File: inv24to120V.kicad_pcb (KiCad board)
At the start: 2 copper layers, 237.5 x 150 mm, 161 parts, among them J1 0705530003, J10 Screw_Terminal_01x01, J12 Screw_Terminal_01x01, J2 Conn_01x02, J3 Conn_01x02, J7 Screw_Terminal_01x03, Q1 IRFZ44NPBF, Q2 IRFZ44NPBF, Q3 ZXTN2010ZTA, Q4 ZXTN2010ZTA, Q5 ZXTP2012ZTA, Q6 ZXTP2012ZTA, SW1 SW_DIP_x02, U1 ESP32-DEVKITC-32D, U10 FOD817A, U11 ACT45B-220-2P-TL003, U12 LM2576R-5.0, U13 FOD817A, U14 KIA7805AF, U15 FOD817A, U2 LM2576R-5.0, U3 ACS712ELCTR30AT, U4 ACS712ELCTR30AT, U6 ISO7340CDW, U7 ISO7340CDW, U8 AMC1300BDWVR, U9 TJA1040T

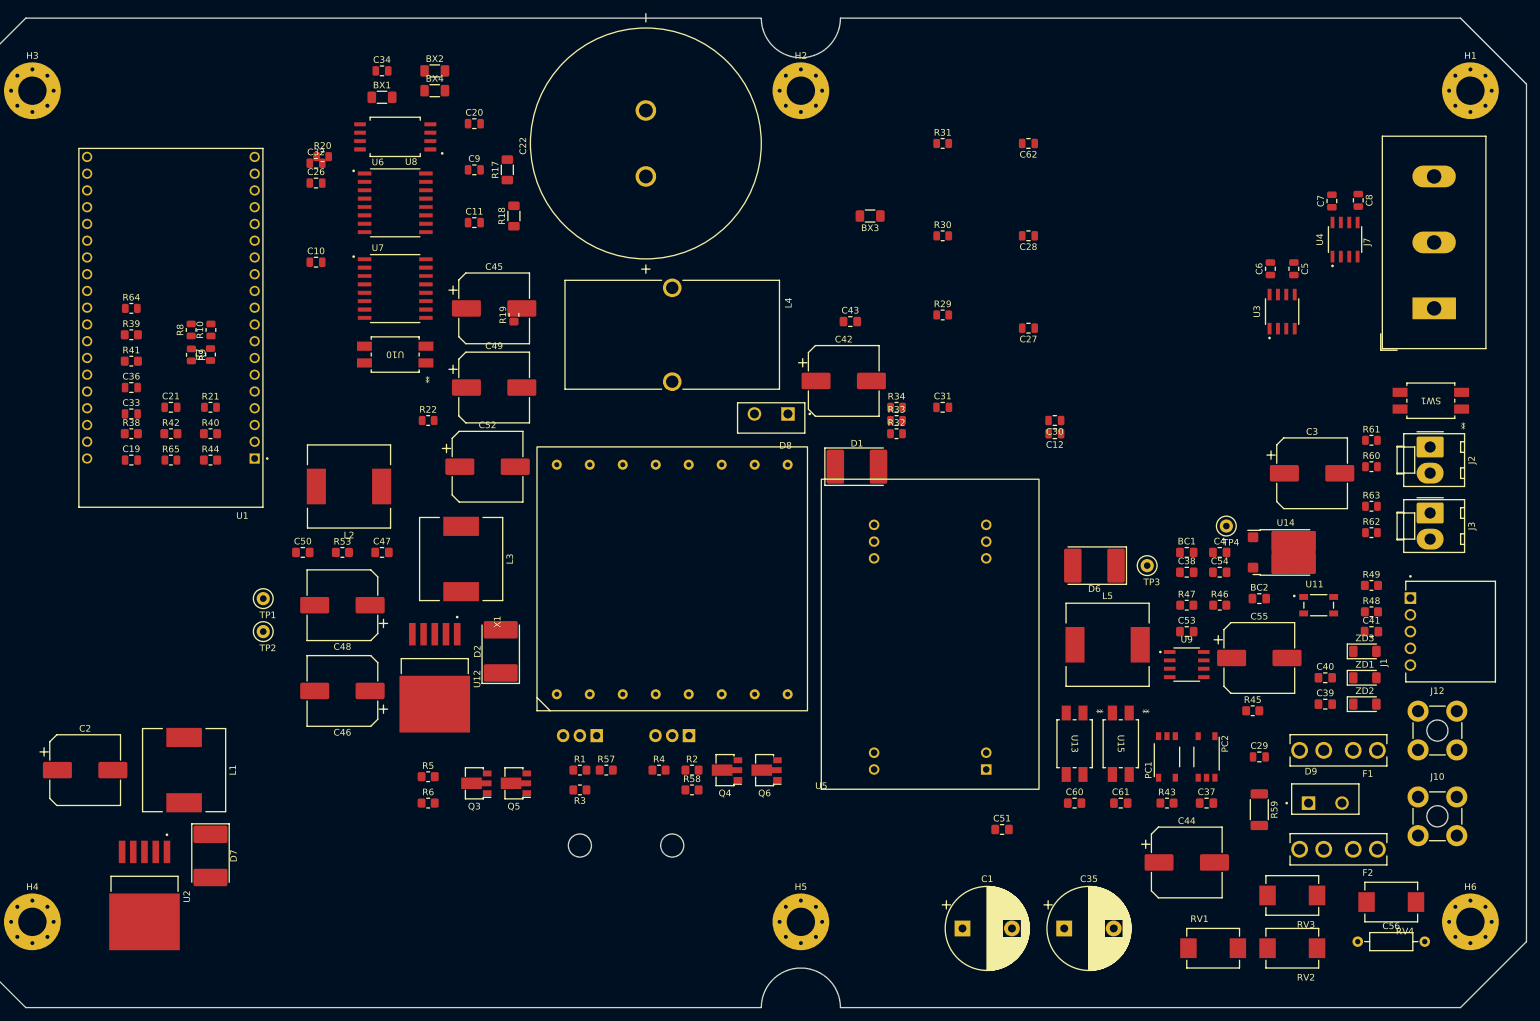
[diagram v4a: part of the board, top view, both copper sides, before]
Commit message: non isolate inverter place parts,
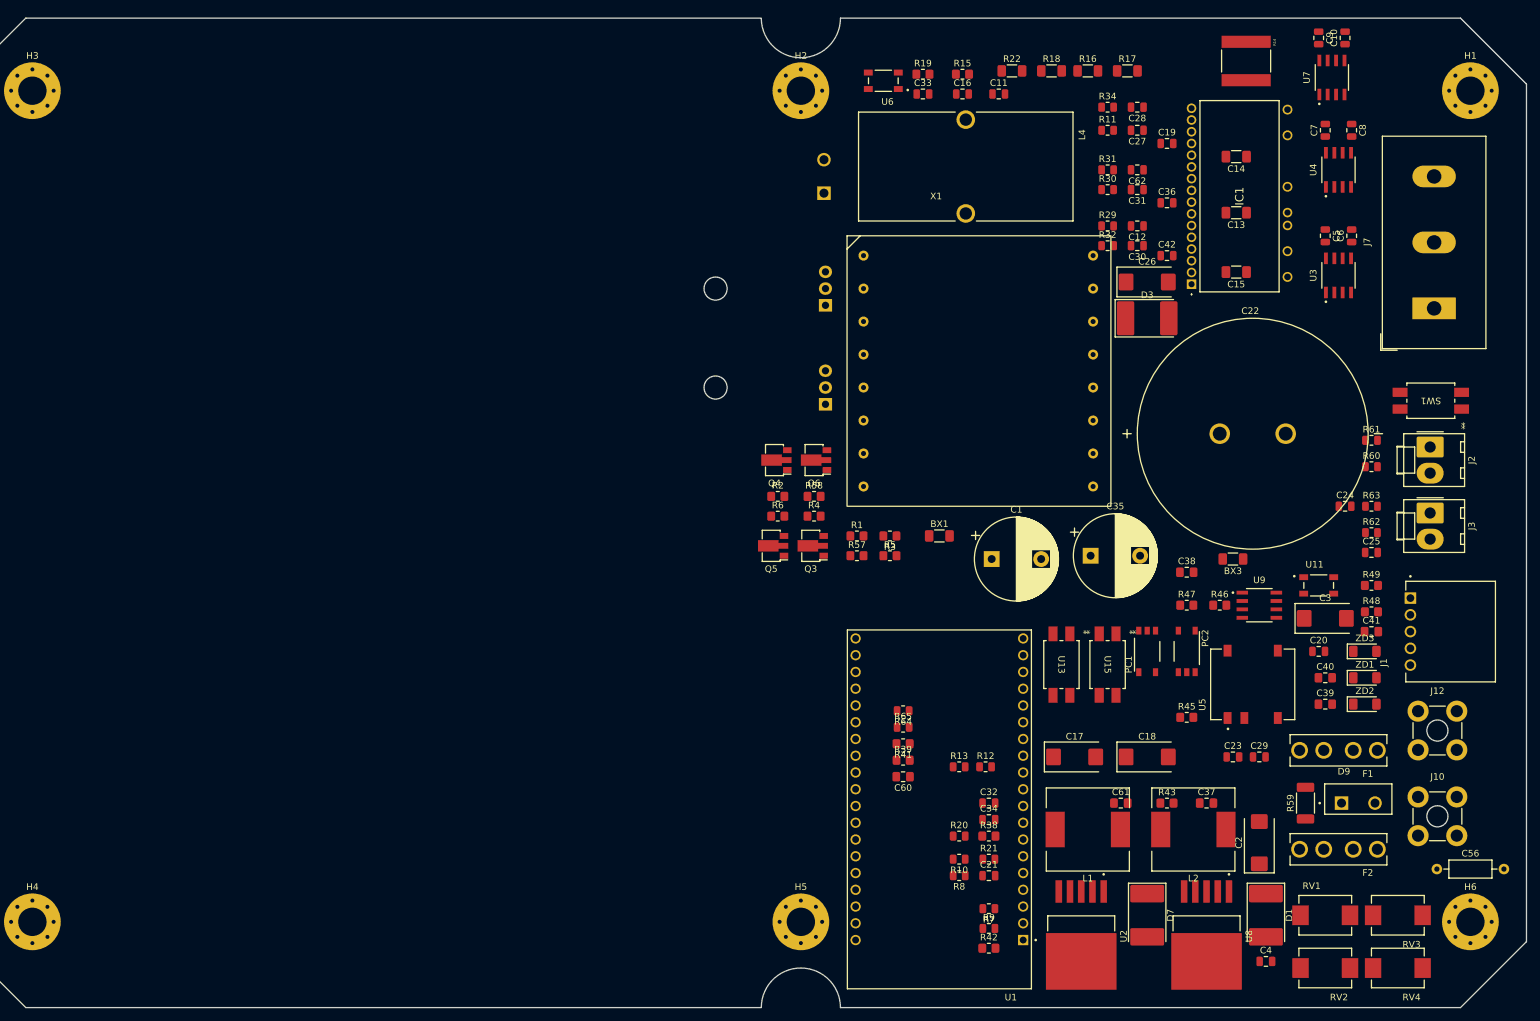
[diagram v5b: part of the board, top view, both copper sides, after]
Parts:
- removed BC1, BC2, C43, C47, C50, C51, C54: 104, Capacitor_SMD:C_0805_2012Metric_Pad1.18x1.45mm_HandSolder
- removed BX2, BX4: BLM31KN801SH1L, Resistor_SMD:R_1206_3216Metric_Pad1.30x1.75mm_HandSolder
- removed C44, C45, C46, C48, C49: 470uF/25V, Capacitor_SMD:CP_Elec_10x12.5
- removed C52, C55: 220uF/50V, Capacitor_SMD:CP_Elec_10x12.5
- removed C53: 334, Capacitor_SMD:C_0805_2012Metric_Pad1.18x1.45mm_HandSolder
- removed D2, D6: SS16, Diode_SMD:D_3220_8050Metric_Pad2.65x5.15mm_HandSolder
- removed L3, L5: 100uH, Inductor_SMD:L_12x12mm_H8mm
- removed R33: 100, Resistor_SMD:R_0805_2012Metric
- removed R40: 10K, Resistor_SMD:R_0805_2012Metric_Pad1.20x1.40mm_HandSolder
- removed R44: 4.7K, Resistor_SMD:R_0805_2012Metric_Pad1.20x1.40mm_HandSolder
- removed R53: 1k, Resistor_SMD:R_0805_2012Metric_Pad1.20x1.40mm_HandSolder
- removed TP1, TP2, TP3, TP4: TestPoint, TestPoint:TestPoint_Loop_D2.50mm_Drill1.0mm
- removed U10: FOD817A, inv24VLib:PDIP4GW_709AH_ONS-M
- removed U12: LM2576R-5.0, genCtrlPCB_Lib:VREG_TPS79625KTTR
- removed U14: KIA7805AF, Package_TO_SOT_SMD:ATPAK-2
- added C13: 10uF, Capacitor_SMD:C_1206_3216Metric_Pad1.33x1.80mm_HandSolder, F.Cu at (223.5, 44.5)
- added C14: 10uF, Capacitor_SMD:C_1206_3216Metric_Pad1.33x1.80mm_HandSolder, F.Cu at (223.5, 36.0)
- added C15: 10uF, Capacitor_SMD:C_1206_3216Metric_Pad1.33x1.80mm_HandSolder, F.Cu at (223.5, 53.5)
- added C16: 102, Capacitor_SMD:C_0805_2012Metric, F.Cu at (182.0, 26.5)
- added C17: 22uF/25V TCSCS1E226MDAR, Capacitor_Tantalum_SMD:CP_EIA-7343-31_Kemet-D_Pad2.25x2.55mm_HandSolder, F.Cu at (199.0, 127.0)
- added C18: 22uF/25V TCSCS1E226MDAR, Capacitor_Tantalum_SMD:CP_EIA-7343-31_Kemet-D_Pad2.25x2.55mm_HandSolder, F.Cu at (210.0, 127.0)
- added C23: 104, Capacitor_SMD:C_0805_2012Metric, F.Cu at (223.0, 127.0)
- added C24: 104, Capacitor_SMD:C_0805_2012Metric, F.Cu at (240.0, 89.0)
- added C25: 104, Capacitor_SMD:C_0805_2012Metric, F.Cu at (244.0, 96.0)
- added D3: SS16, Diode_SMD:D_3220_8050Metric_Pad2.65x5.15mm_HandSolder, F.Cu at (210.0, 60.5)
- added IC1: NFA50460R4B, kilib:NFA50460R4B, F.Cu at (216.7, 55.3)
- added R11: 100, Resistor_SMD:R_0805_2012Metric, F.Cu at (204.0, 32.0)
- added R12: 2K, Resistor_SMD:R_0805_2012Metric, F.Cu at (185.5, 128.5)
- added R13: 2K, Resistor_SMD:R_0805_2012Metric, F.Cu at (181.5, 128.5)
- added R14: CSS2728JT40L0, kilib:RESC6771X124N, F.Cu at (225.0, 21.5)
- added R15: 1k, Resistor_SMD:R_0805_2012Metric_Pad1.20x1.40mm_HandSolder, F.Cu at (182.0, 23.5)
- added R16: 51K, Resistor_SMD:R_1206_3216Metric_Pad1.30x1.75mm_HandSolder, F.Cu at (201.0, 23.0)
- C10, C11: value 104 -> 102
- C19, C36: value 104 -> 10uF
- C2, C3: value 470uF/25V -> 22uF/25V TCSCS1E226MDAR; footprint Capacitor_SMD:CP_Elec_10x12.5 -> Capacitor_Tantalum_SMD:CP_EIA-7343-31_Kemet-D_Pad2.25x2.55mm_HandSolder
- C26: value 104 -> 22uF/25V TCSCS1E226MDAR; footprint Capacitor_SMD:C_0805_2012Metric -> Capacitor_Tantalum_SMD:CP_EIA-7343-31_Kemet-D_Pad2.25x2.55mm_HandSolder
- C4: footprint Capacitor_SMD:C_0805_2012Metric_Pad1.18x1.45mm_HandSolder -> Capacitor_SMD:C_0805_2012Metric
- C42: value 470uF/25V -> 10uF; footprint Capacitor_SMD:CP_Elec_10x12.5 -> Capacitor_SMD:C_0805_2012Metric
- D8: moved to B.Cu
- R17, R18: value 1M/2W -> 51K
- R22: value 470 -> 51K; footprint Resistor_SMD:R_0805_2012Metric -> Resistor_SMD:R_1206_3216Metric_Pad1.30x1.75mm_HandSolder
- U5: footprint Library:ewDCDC24_1505d -> kilib:CONV_R1SE-0505
- U6: value ISO7340CDW -> ACT45B-220-2P-TL003; footprint inv24VLib:SOIC127P1030X265-16N -> genCtrlPCB_Lib:FIL_ACT45B-220-2P-TL003
- U7: value ISO7340CDW -> ACS712ELCTR30AT; footprint inv24VLib:SOIC127P1030X265-16N -> inv24VLib:SOIC127P600X175-8N
- U8: value AMC1300BDWVR -> LM2576R-15.0; footprint inv24VLib:SOIC127P1150X280-8N -> genCtrlPCB_Lib:VREG_TPS79625KTTR
- moved C2 178.3 mm to (227.0, 140.0), turned to 90 degrees
- moved U8 175.4 mm to (219.0, 158.0), turned to -90 degrees
- moved C19 164.2 mm to (213.0, 34.0)
- moved C10 159.7 mm to (240.0, 18.0), turned to 90 degrees
- moved C36 159.5 mm to (213.0, 43.0)
- moved C20 150.9 mm to (236.0, 111.0)
- moved R9 148.9 mm to (186.0, 153.0), turned to 0 degrees
- moved R42 146.5 mm to (186.0, 156.0)
- moved C34 146.1 mm to (186.0, 136.5)
- moved U7 145.6 mm to (238.0, 24.0), turned to 90 degrees
- moved R7 144.8 mm to (186.0, 150.0), turned to 180 degrees
- moved R38 143.6 mm to (186.0, 139.0)
- moved C21 142.9 mm to (186.0, 145.0)
- moved R8 142.8 mm to (181.5, 145.0), turned to 180 degrees
- moved D7 142.3 mm to (210.0, 151.0)
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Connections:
- net IN_WH renamed Net-(IC1-LIN(V))
- BX1 pad 1: +5V -> GNDPWR
- BX1 pad 2: VTH_IPM -> GND
- BX3 pad 1: GND2 -> GND
- C10 pad 1: +3.3V -> Net-(U7-FILTER)
- C11 pad 1: GND2 -> GND
- C11 pad 2: +5VP -> VTS
- C12 pad 1: GND2 -> GND
- C12 pad 2: IN_UL -> Net-(IC1-HIN(U))
- C19 pad 2: VDC_IN -> +15V
- C2 pad 1: +5V -> +15V
- C20 pad 1: +5VP -> GND1
- C20 pad 2: GND2 -> +5P
- C26 pad 1: +3.3V -> +15V
- C27 pad 1: GND2 -> GND
- C27 pad 2: IN_UH -> Net-(IC1-HIN(W))
- C28 pad 1: GND2 -> GND
- C28 pad 2: IN_VH -> Net-(IC1-LIN(W))
- C3 pad 1: +8VP_IN -> +5V
- C3 pad 2: GND1 -> GND
- C30 pad 1: GND2 -> GND
- C30 pad 2: IN_VL -> Net-(IC1-LIN(U))
- C31 pad 1: GND2 -> GND
- C31 pad 2: IN_WL -> Net-(IC1-HIN(V))
- C32 pad 2: +5V -> Net-(C32-Pad2)
- C33 pad 1: Net-(BX2-Pad2) -> GNDPWR
- C33 pad 2: VTH_IPM -> Net-(C33-Pad2)
- C34 pad 2: TEMPERATURE_IPM -> 24V_IN
- C36 pad 2: +5V -> +15V
- C4 pad 1: +8VP_IN -> GND
- C4 pad 2: GND1 -> +24V
- C42 pad 1: 15V_H_IN -> GND
- C42 pad 2: GND2 -> +15V
- C62 pad 1: GND2 -> GND
- C9 pad 1: +5VP -> GND
- C9 pad 2: GND2 -> +5V
- D1 pad 2: 15V_H_IN -> GND
- L2 pad 1: Net-(D2-K) -> Net-(D1-K)
- L2 pad 2: +5VP -> +15V
- R17 pad 1: Net-(R17-Pad1) -> VBUS
- R17 pad 2: VBUS -> Net-(R16-Pad2)
- R18 pad 1: Net-(U8-INP) -> Net-(R16-Pad1)
- R18 pad 2: Net-(R17-Pad1) -> Net-(R18-Pad2)
- R19 pad 2: Net-(U8-INP) -> Net-(C33-Pad2)
- R20 pad 2: Net-(U8-OUTP) -> Net-(C32-Pad2)
- R22 pad 1: Net-(R22-Pad1) -> Net-(C33-Pad2)
- R22 pad 2: +5VP -> Net-(R18-Pad2)
- R29 pad 1: UH1 -> PWM1_H
- R29 pad 2: IN_UH -> Net-(IC1-HIN(U))
- R30 pad 1: VH1 -> PWM2_H
- R30 pad 2: IN_VH -> Net-(IC1-HIN(V))
- R31 pad 1: WH1 -> PWM2_L
- R32 pad 1: UL1 -> PWM1_L
- R32 pad 2: IN_UL -> Net-(IC1-LIN(U))
- R34 pad 1: WL1 -> PWM3_L
- R34 pad 2: IN_WL -> Net-(IC1-LIN(W))
- R38 pad 2: VDC_IN -> 24V_IN
- U1 pad J2-6: ANALOG_CMD -> I_DC
- U1 pad J2-7: TEMPERATURE_IPM -> VTS
- U1 pad J2-8: VDC_IN -> 24V_IN
- U5 pad 1: +24V -> GND
- U5 pad 2: GND -> +5V
- U5 pad 4: unconnected-(U5-NC2-Pad4) -> GND1
- U5 pad 5: unconnected-(U5-Vout1-Pad5) -> +5P
- U5 pad 8: 15V_H_IN -> unconnected-(U5-NC-Pad8)
- U6 pad 1: +3.3V -> Net-(C33-Pad2)
- U6 pad 2: GND -> GNDPWR
- U6 pad 3: PWM0_H -> GND
- U6 pad 4: PWM1_H -> Net-(C32-Pad2)
- U7 pad 1: +3.3V -> I_DC_IN
- U7 pad 2: GND -> I_DC_IN
- U7 pad 3: PWM0_L -> GNDPWR
- U7 pad 4: PWM1_L -> GNDPWR
- U7 pad 5: PWM2_L -> GND
- U7 pad 6: GND -> Net-(U7-FILTER)
- U7 pad 7: (no net) -> Net-(U7-VIOUT)
- U7 pad 8: GND -> +5V
- U8 pad 1: +5VP -> GND
- U8 pad 2: Net-(U8-INP) -> Net-(D1-K)
- U8 pad 3: GNDPWR -> GND
- U8 pad 4: GND2 -> +15V
- U8 pad 5: GND -> +24V

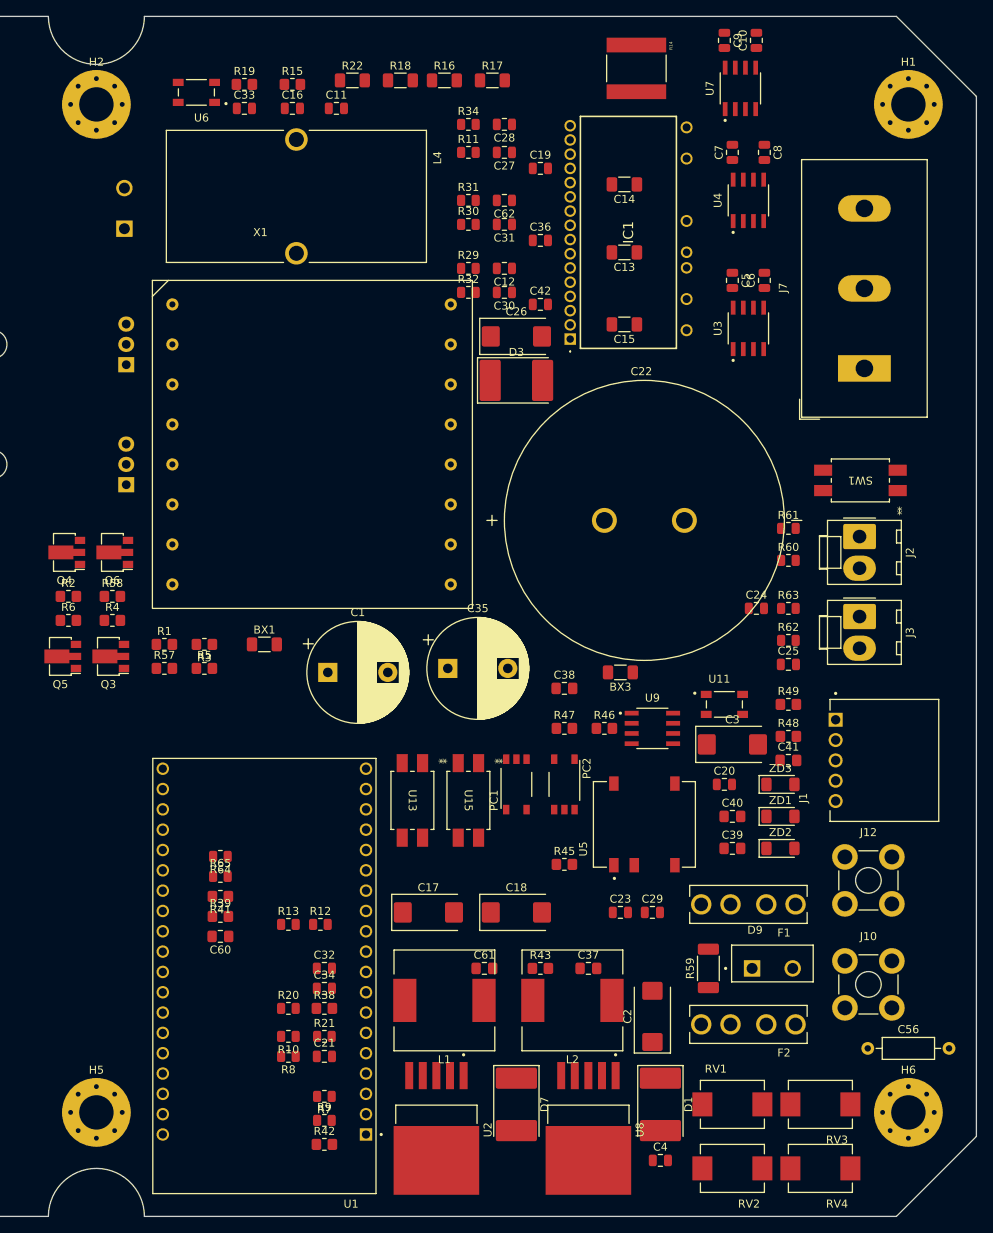
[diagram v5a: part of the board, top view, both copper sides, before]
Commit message: fix 35313-0460 0260 dip se 3d model
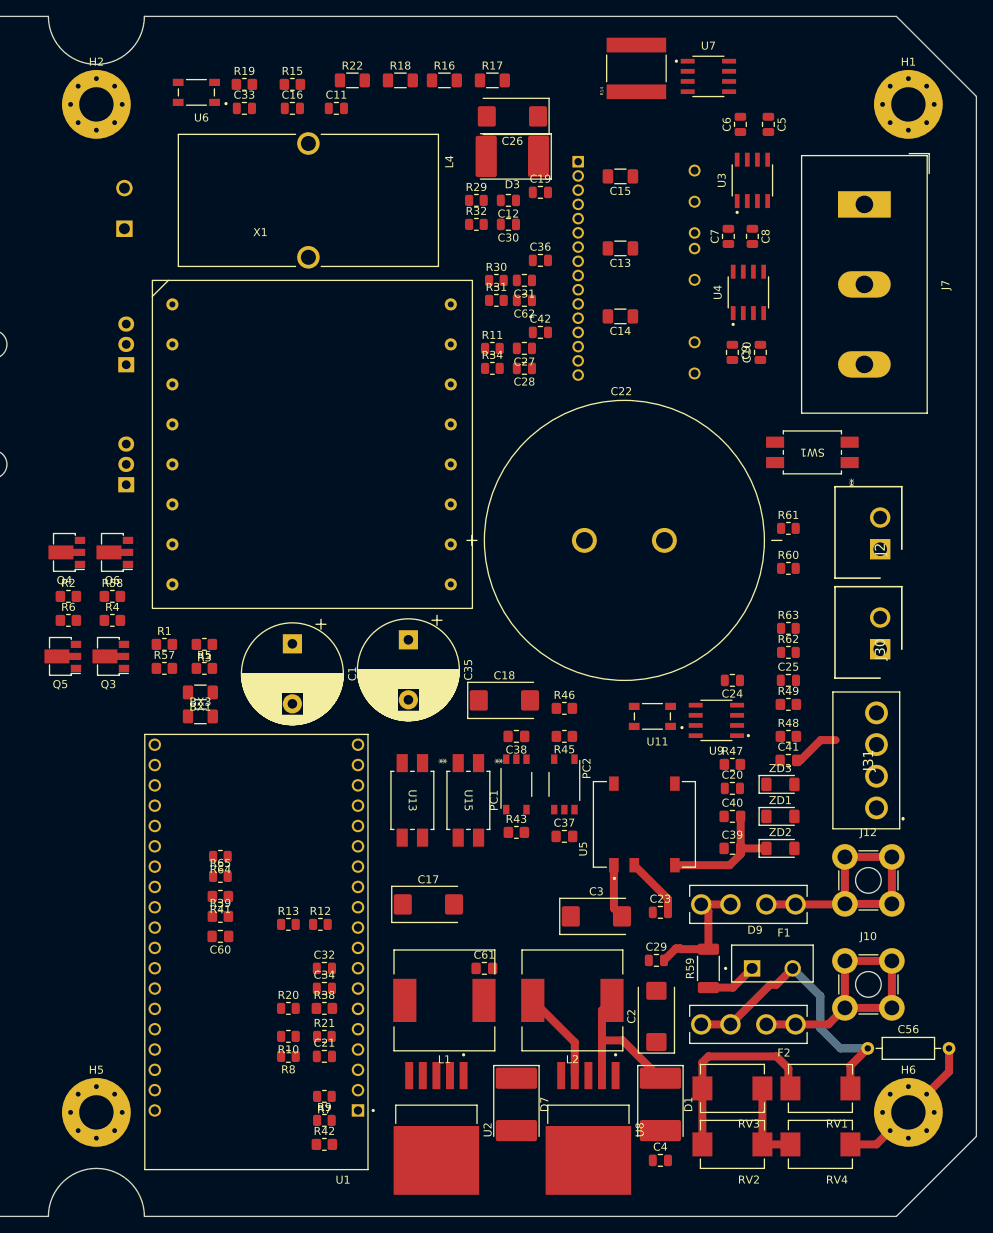
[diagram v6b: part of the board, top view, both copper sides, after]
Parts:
- removed J1: 0705530003, genCtrlPCB_Lib:MOLEX_0705530039
- removed J3: Conn_01x02, Connector_Molex:Molex_KK-396_A-41791-0002_1x02_P3.96mm_Vertical
- added J30: 35313-0260, kilib:SHDR2W107P0X396_1X2_1118X835X1000P, F.Cu at (255.5, 94.1)
- added J31: 35313-0460, kilib:353130460, F.Cu at (255.3, 113.8)
- IC1: moved to B.Cu
- J2: value Conn_01x02 -> 35313-0260; footprint Connector_Molex:Molex_KK-396_A-41791-0002_1x02_P3.96mm_Vertical -> kilib:SHDR2W107P0X396_1X2_1118X835X1000P
- moved BX3 52.8 mm to (170.5, 102.5), turned to 0 degrees
- moved C9 39.0 mm to (237.0, 57.0)
- moved C10 39.0 mm to (240.5, 57.0)
- moved R34 30.6 mm to (207.0, 59.0)
- moved C28 30.6 mm to (211.0, 59.0)
- moved D3 28.0 mm to (209.5, 32.5), turned to 180 degrees
- moved C26 27.5 mm to (209.5, 27.5), turned to 180 degrees
- moved C3 27.4 mm to (220.0, 127.5)
- moved C18 26.5 mm to (208.5, 100.5)
- moved R11 24.7 mm to (207.0, 56.5)
- moved C27 24.6 mm to (211.0, 56.5)
- moved IC1 22.2 mm to (217.7, 33.2), turned to -90 degrees
- moved R47 21.5 mm to (237.0, 108.5)
- moved J7 20.5 mm to (253.5, 38.5), turned to -90 degrees
- moved C5 20.0 mm to (241.5, 28.5)
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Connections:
- C24 pad 2: Net-(J2-Pin_2) -> Net-(C24-Pad2)
- C25 pad 2: Net-(J3-Pin_2) -> Net-(C25-Pad2)
- J2 pad 2: Net-(J2-Pin_2) -> Net-(C25-Pad2)
- R60 pad 2: Net-(J2-Pin_2) -> Net-(C24-Pad2)
- R62 pad 2: Net-(J3-Pin_2) -> Net-(C25-Pad2)
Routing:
- net GND: track 0.00 -> 42.9 mm
- net +24V: track 0.00 -> 40.4 mm
- net Net-(J10-Pin_1): track 0.00 -> 34.2 mm
- net Net-(J12-Pin_1): track 0.00 -> 33.3 mm
- net GND1: track 0.00 -> 22.7 mm
- net Net-(D1-K): track 0.00 -> 19.2 mm
- net Earth: track 0.00 -> 19.0 mm
- net +15V: track 0.00 -> 11.6 mm
- net Net-(RV2-Pad1): track 0.00 -> 10.5 mm
- net +5V: track 0.00 -> 7.65 mm
- net Net-(D9-K): track 0.00 -> 6.46 mm
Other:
- outline, holes or cut-outs redrawn
- board text added: "GND DC+"
- board text added: "U V W"
